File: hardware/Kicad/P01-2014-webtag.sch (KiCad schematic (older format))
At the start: 4 parts

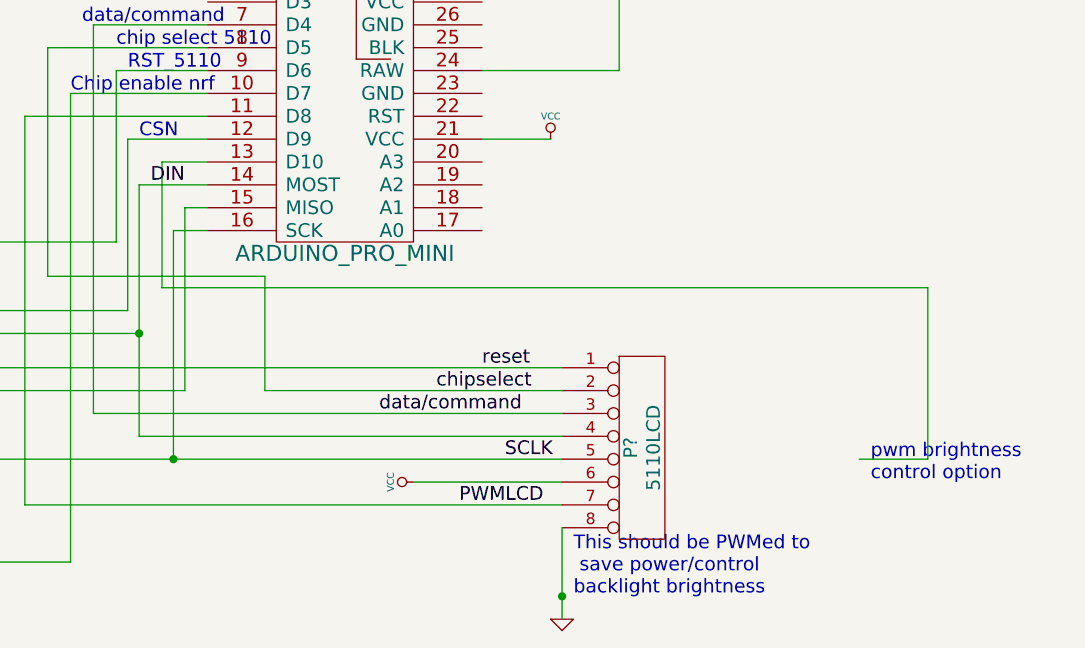
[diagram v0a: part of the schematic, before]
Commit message: update pins and pwm connection
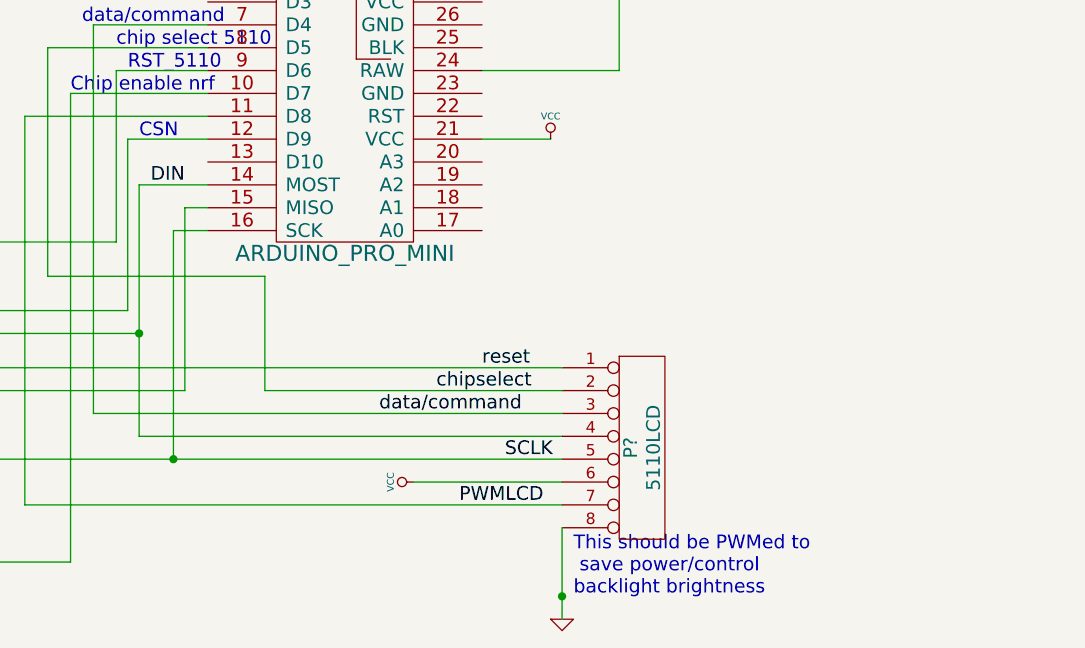
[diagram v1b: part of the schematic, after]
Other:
- note removed: "pwm brightness \ncontrol option"
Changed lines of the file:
@@
 Text Notes 6650 4600 0    60   ~ 0
 This should be PWMed to\n save power/control \nbacklight brightness
-Text Notes 7950 4100 0    60   ~ 0
-pwm brightness \ncontrol option
 $Comp
 L CONN_4X2 P?
@@
 	6650 1350 6650 1500
 Wire Wire Line
-	5050 2700 4850 2700
-Wire Wire Line
-	4850 2700 4850 3250
-Wire Wire Line
-	4850 3250 8200 3250
-Wire Wire Line
-	8200 3250 8200 4000
-Wire Wire Line
-	8200 4000 7900 4000
-Wire Wire Line
 	3300 3250 3300 3100
